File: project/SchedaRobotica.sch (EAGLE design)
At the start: 63 parts, among them IC1 LMZ14202TZE-ADJ_NOPB, IC2 VNH7070ASTR, IC3 VNH7070ASTR, IC4 VNH7070ASTR, IC5 VNH7070ASTR

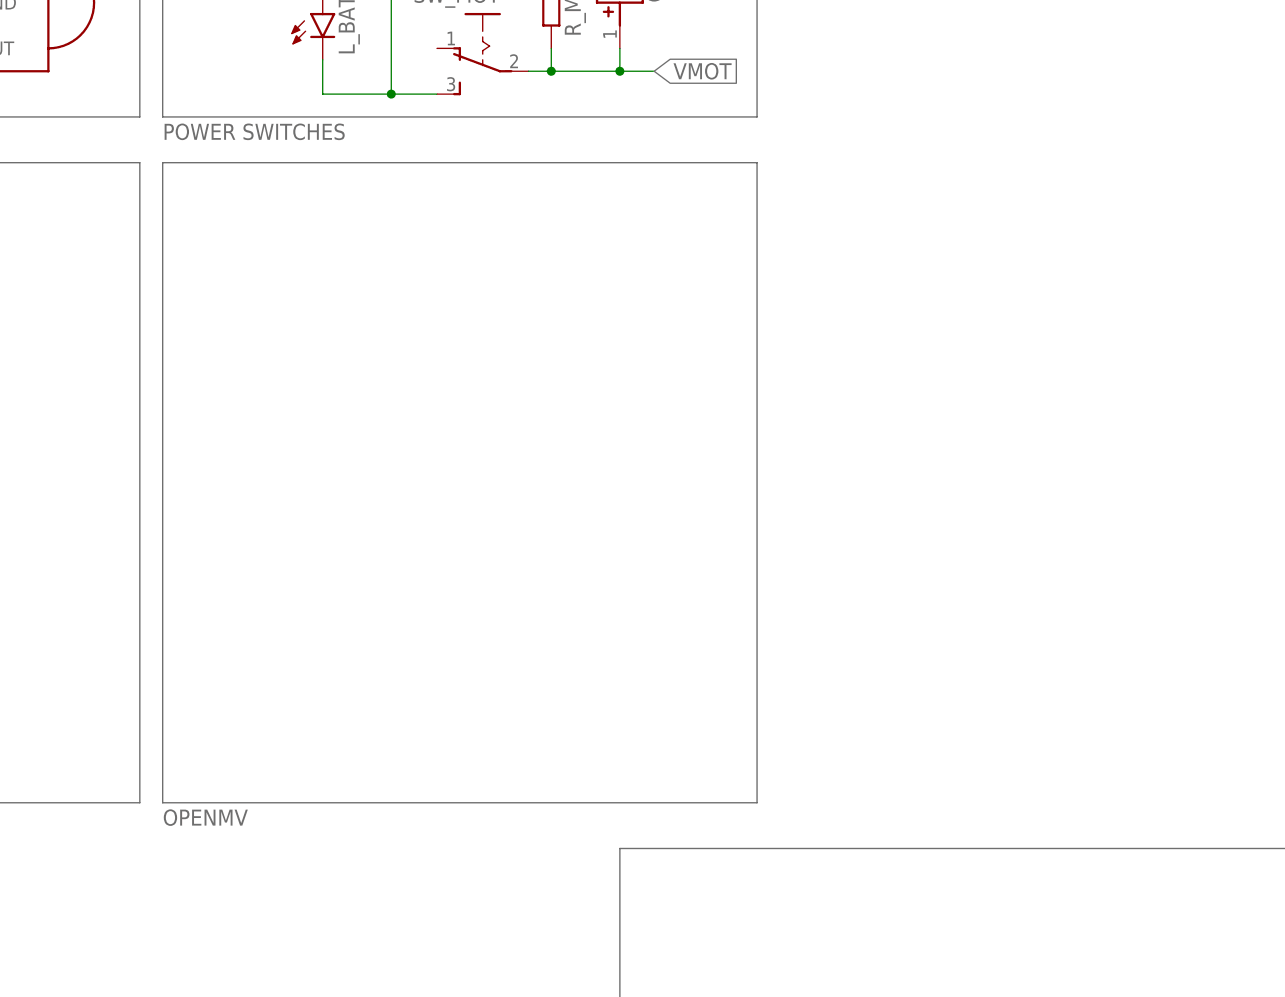
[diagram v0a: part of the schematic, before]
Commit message: added camera and motor cons
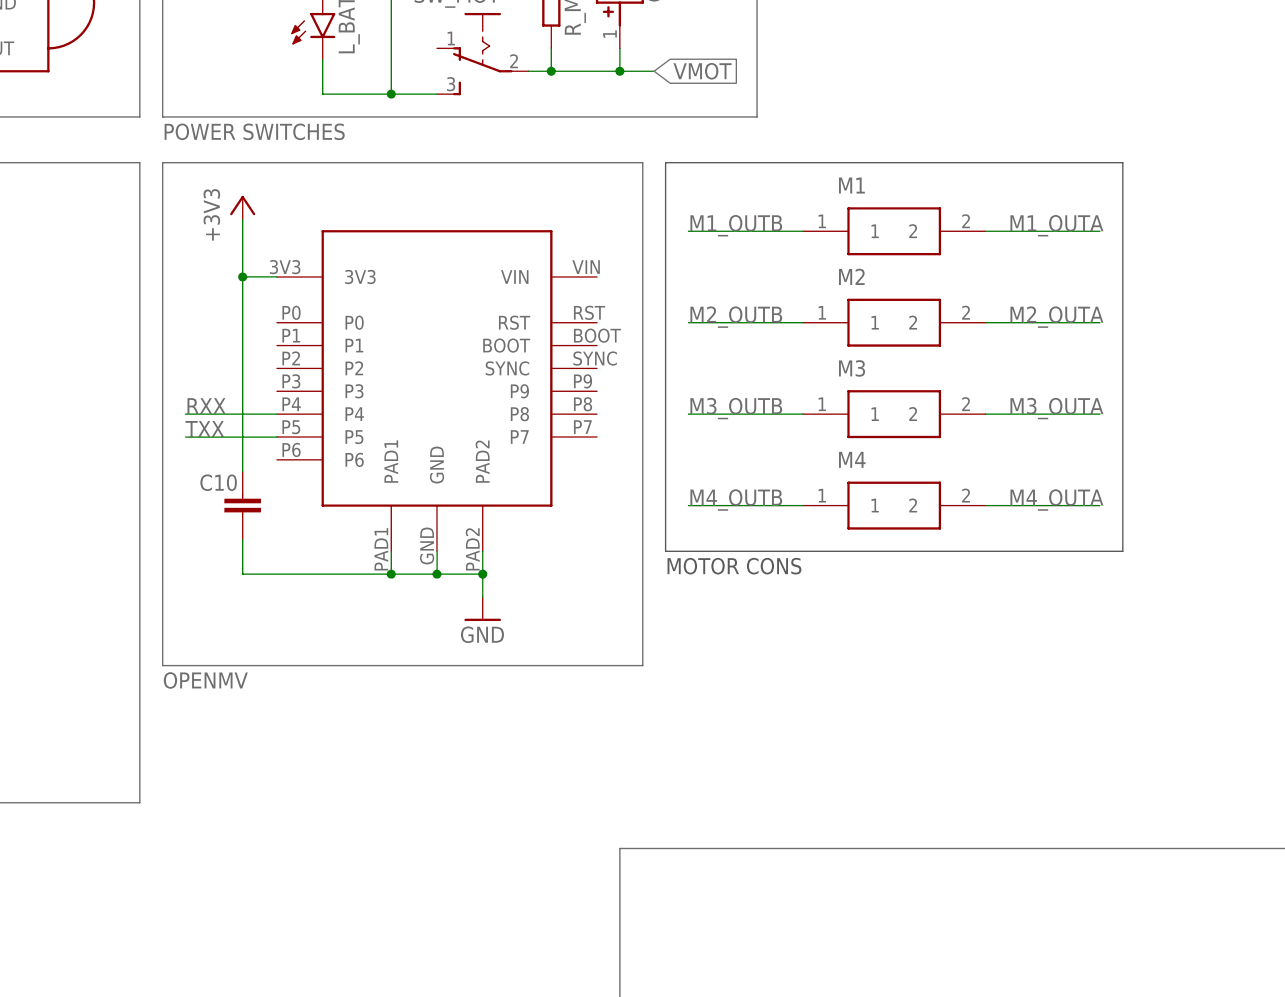
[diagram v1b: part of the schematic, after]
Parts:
- added C10: 100u, rcl:C-EUC1206
- added M1, M2, M3, M4: 43650-0201, Molex motori:43650-0201
- added U$2: OPENMV_H7, OpenMV:OPENMV_H7
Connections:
- new net M1_OUTA: M1.2
- new net M1_OUTB: M1.1
- new net M2_OUTA: M2.2
- new net M2_OUTB: M2.1
- new net M3_OUTA: M3.2
- new net M3_OUTB: M3.1
- new net M4_OUTA: M4.2
- new net M4_OUTB: M4.1
- new net RXX: U$2.P4
- new net TXX: U$2.P5
- net +3V3: now also C10.1, U$2.3V3
- net GND: now also C10.2, U$2.GND, U$2.PAD1, U$2.PAD2
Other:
- note added: "MOTOR CONS"

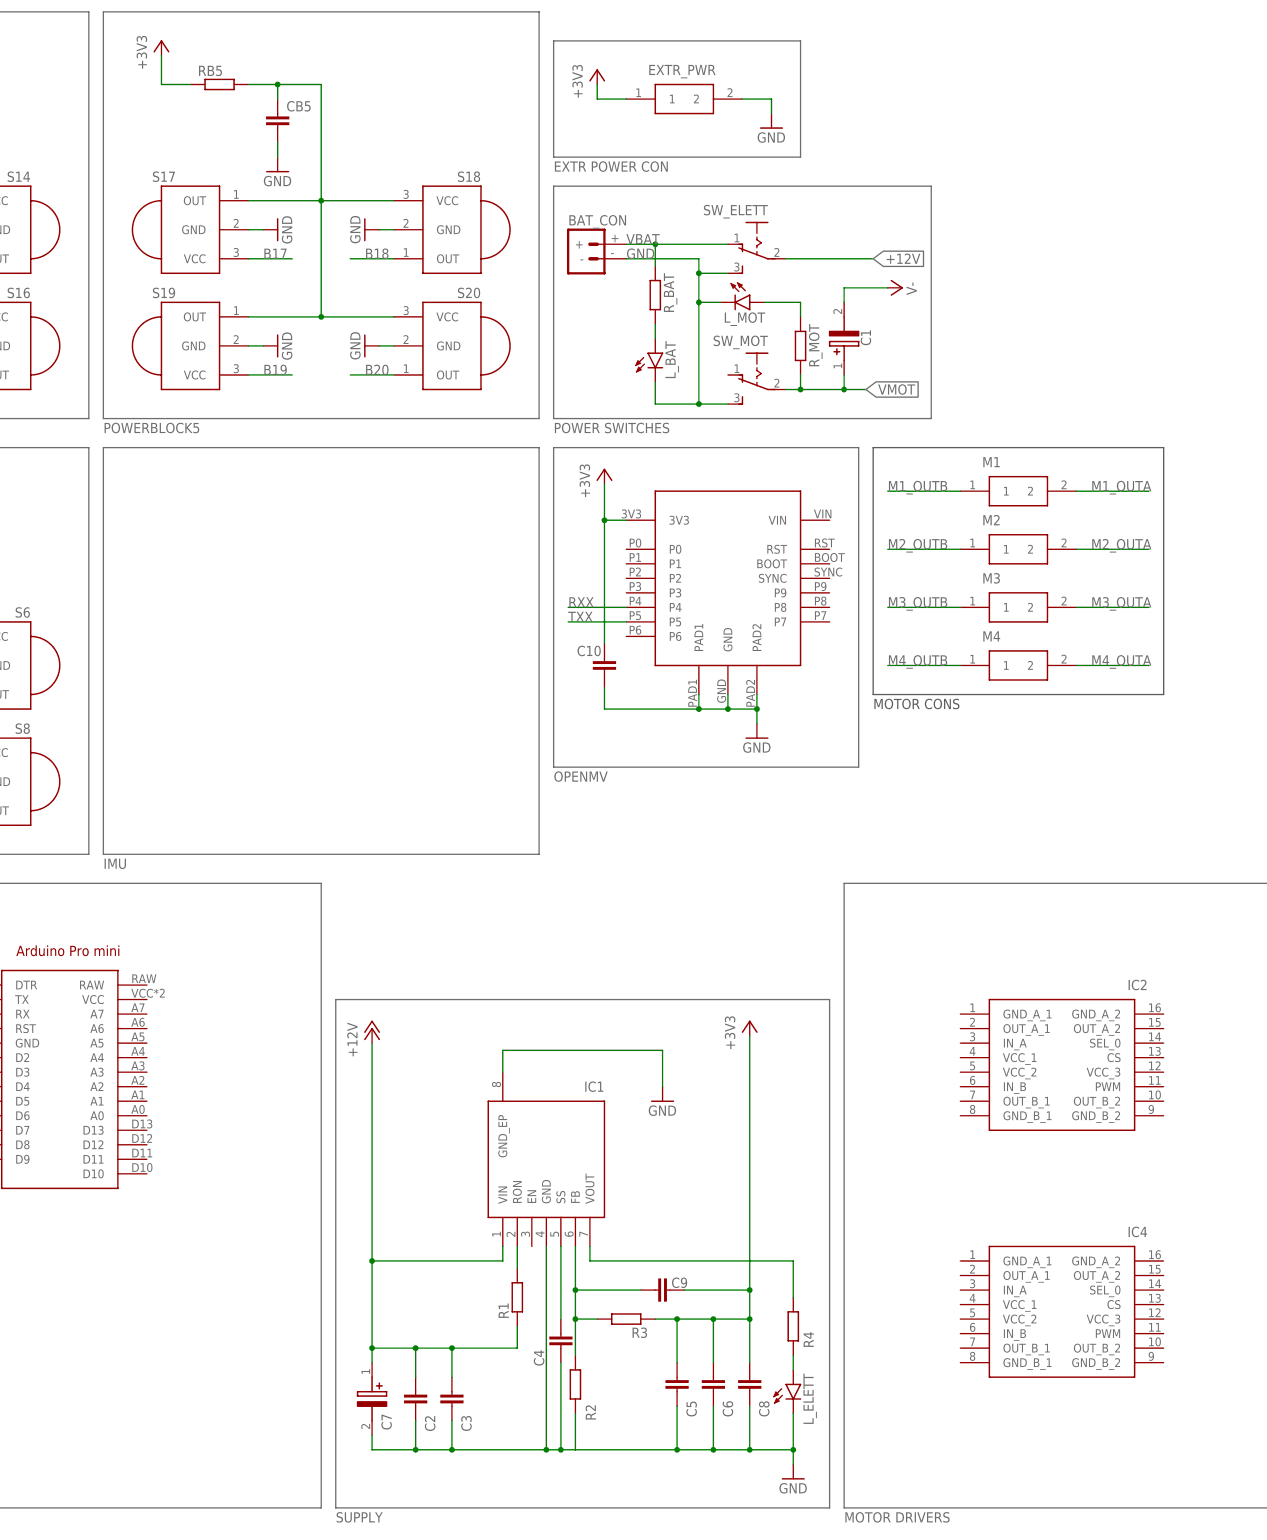
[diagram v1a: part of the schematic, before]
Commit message: integrated new libs, added a todo and line sensors
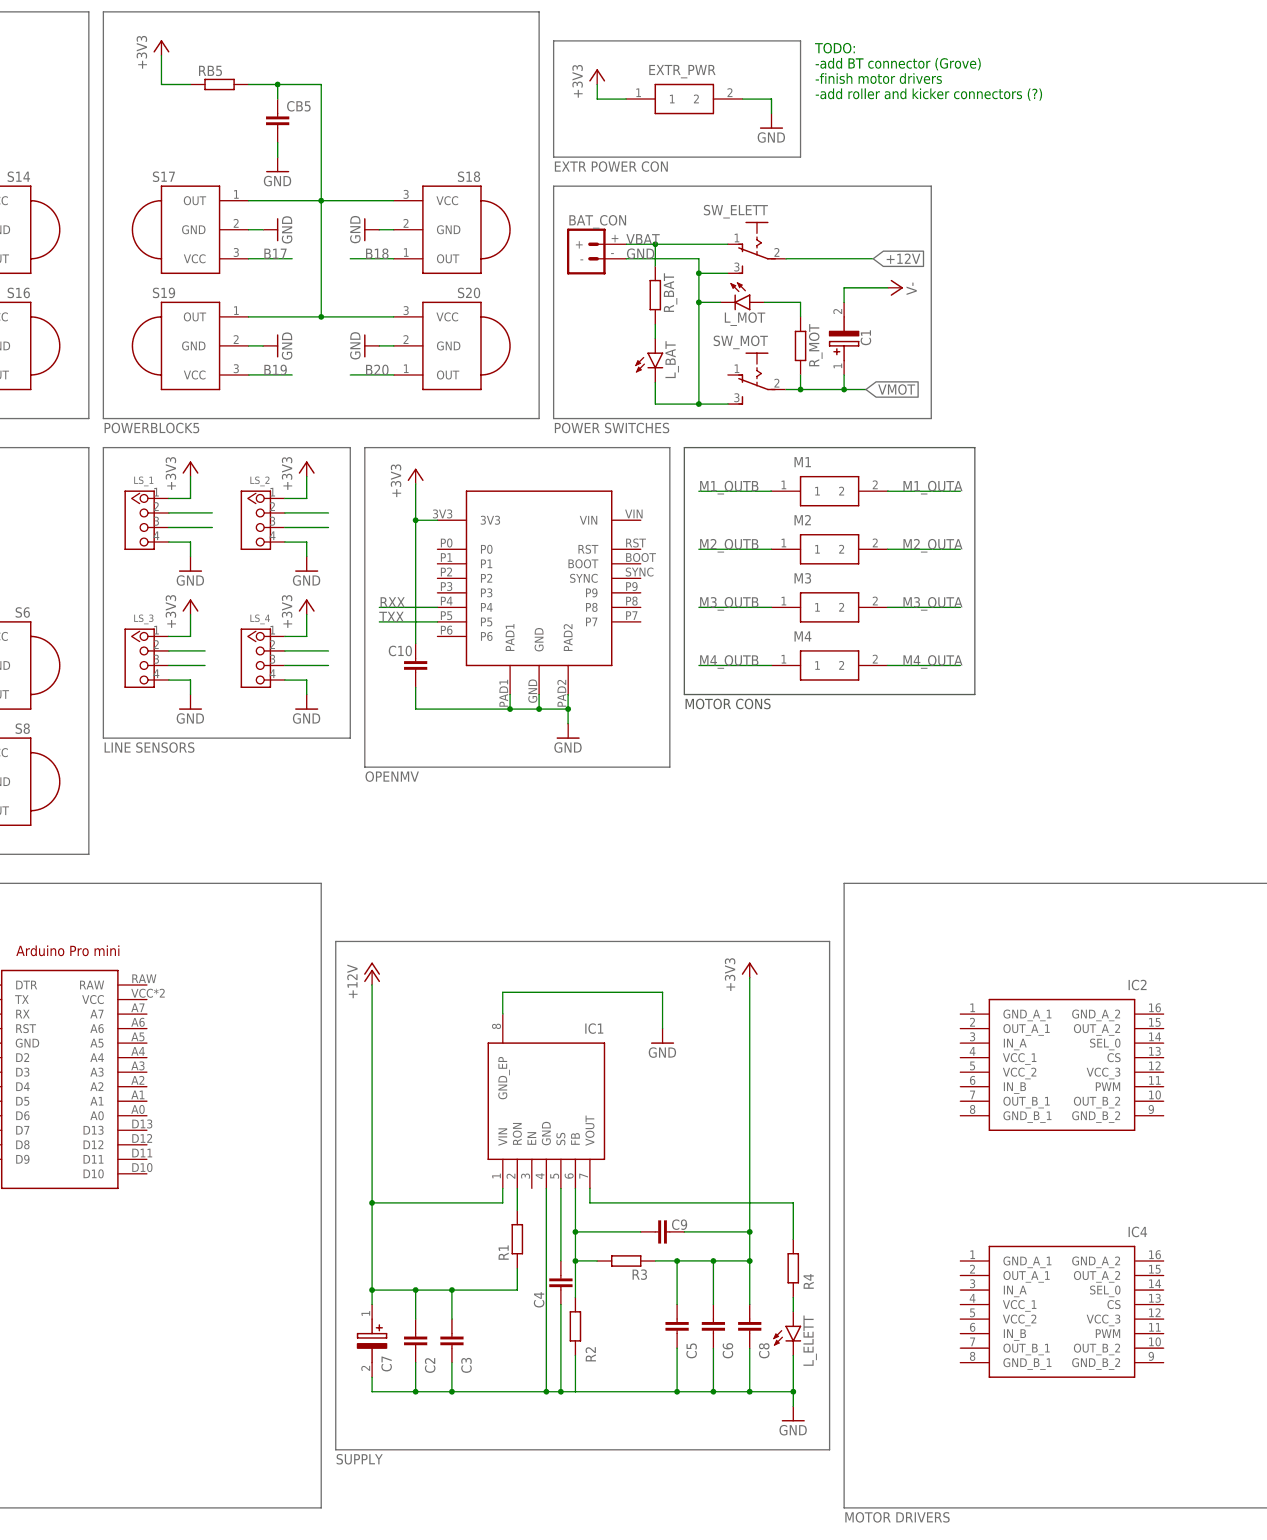
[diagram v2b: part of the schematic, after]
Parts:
- added LS_1, LS_2, LS_3, LS_4: 4P-2.0, OPL_Connector:GROVE-CONNECTOR-DIP(4P-2.0)
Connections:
- new net N$13: LS_3.3
- new net N$15: LS_1.2
- new net N$16: LS_1.3
- new net N$17: LS_2.2
- new net N$18: LS_2.3
- new net N$19: LS_4.2
- new net N$20: LS_4.3
- new net N$8: LS_3.2
- net +3V3: now also LS_1.1, LS_2.1, LS_3.1, LS_4.1
- net GND: now also LS_1.4, LS_2.4, LS_3.4, LS_4.4
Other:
- note added: "LINE SENSORS"
- note added: "TODO: -add BT connector (Grove) -finish motor drivers -add roller and kicker connectors (?)"
- note removed: "IMU"
- moved on the sheet: C10, C2, C3, C4, C5, C6, C7, C8, C9, IC1, L_ELETT, M1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
